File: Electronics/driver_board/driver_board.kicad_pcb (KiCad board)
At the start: 4 copper layers, 0 parts

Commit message: Initial placement
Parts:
- added C1: 0.1u, Capacitor_SMD:C_0402_1005Metric, F.Cu at (77.5, 67.5)
- added C11: 0.1u 150V, Capacitor_SMD:C_0805_2012Metric, F.Cu at (60.5, 123.5)
- added C18: 0.1u 150V, Capacitor_SMD:C_0805_2012Metric, F.Cu at (55.0, 136.0)
- added C2: 4.7u, Capacitor_SMD:C_0603_1608Metric, F.Cu at (91.0, 79.0)
- added C23: 1u, Capacitor_SMD:C_0402_1005Metric, F.Cu at (25.5, 102.0)
- added C24: 0.1u, Capacitor_SMD:C_0402_1005Metric, F.Cu at (27.0, 115.0)
- added C25: 0.1u, Capacitor_SMD:C_0402_1005Metric, F.Cu at (24.5, 93.0)
- added C26: 0.1u, Capacitor_SMD:C_0402_1005Metric, F.Cu at (27.0, 110.0)
- added C27: 1u, Capacitor_SMD:C_0402_1005Metric, F.Cu at (31.5, 102.0)
- added C28: 10u, Capacitor_SMD:C_0805_2012Metric, F.Cu at (32.5, 67.5)
- added C29: 10u, Capacitor_SMD:C_0805_2012Metric, F.Cu at (24.5, 90.0)
- added C3: 0.1u, Capacitor_SMD:C_0402_1005Metric, F.Cu at (77.5, 69.5)
- added C30: 10u, Capacitor_SMD:C_0805_2012Metric, F.Cu at (26.5, 108.5)
- added C31: 4.7u, Capacitor_SMD:C_0603_1608Metric, F.Cu at (160.0, 96.5)
- added C32: 4.7u, Capacitor_SMD:C_0603_1608Metric, F.Cu at (161.5, 108.5)
- added C33: 0.1u, Capacitor_SMD:C_0402_1005Metric, F.Cu at (161.5, 97.0)
- added C34: 0.1u, Capacitor_SMD:C_0402_1005Metric, F.Cu at (163.0, 109.0)
- added C35: 0.1u 150V, Capacitor_SMD:C_0805_2012Metric, F.Cu at (163.0, 90.5)
- added C36: 0.1u 150V, Capacitor_SMD:C_0805_2012Metric, F.Cu at (164.0, 113.0)
- added C37: 0.1u, Capacitor_SMD:C_0402_1005Metric, F.Cu at (187.5, 89.0)
- added C38: 0.1u, Capacitor_SMD:C_0402_1005Metric, F.Cu at (181.5, 82.0)
- added C39: 0.1u, Capacitor_SMD:C_0402_1005Metric, F.Cu at (183.5, 121.5)
- added C4: 0.1u, Capacitor_SMD:C_0402_1005Metric, F.Cu at (77.5, 71.5)
- added C40: 0.1u, Capacitor_SMD:C_0402_1005Metric, F.Cu at (176.5, 84.5)
- added C41: 0.1u, Capacitor_SMD:C_0402_1005Metric, F.Cu at (160.5, 76.0)
- added C5: 0.1u, Capacitor_SMD:C_0402_1005Metric, F.Cu at (77.5, 73.5)
- added C6: 4.7u, Capacitor_SMD:C_0603_1608Metric, F.Cu at (91.0, 81.5)
- added C7: 0.1u, Capacitor_SMD:C_0402_1005Metric, F.Cu at (77.5, 75.5)
- added C8: 0.1u, Capacitor_SMD:C_0402_1005Metric, F.Cu at (77.5, 77.0)
- added D1: SMAJ85A, Diode_SMD:D_SMA, F.Cu at (45.5, 112.0)
- added D2: SMAJ100CA, Diode_SMD:D_SMA, F.Cu at (186.5, 106.5)
- added J1: Conn_ST_STDC14, Connector_PinHeader_1.27mm:PinHeader_2x07_P1.27mm_Vertical_SMD, F.Cu at (63.0, 66.5)
- added NT1: NetTie_2, NetTie:NetTie-2_SMD_Pad0.5mm, F.Cu at (29.5, 115.5)
- added NT2: NetTie_2, NetTie:NetTie-2_SMD_Pad0.5mm, F.Cu at (157.5, 116.0)
- added Q1: IPF036N15NM6, Package_TO_SOT_SMD:TO-263-6, F.Cu at (59.0, 110.5)
- added Q2: IPF036N15NM6, Package_TO_SOT_SMD:TO-263-6, F.Cu at (80.0, 110.5)
- added Q3: IAUZ40N10S5N130, DWlib:Infineon_PG-TSDSON-8-33, B.Cu at (174.5, 95.0)
- added Q4: IAUZ40N10S5N130, DWlib:Infineon_PG-TSDSON-8-33, F.Cu at (176.5, 95.0)
- added Q5: IAUZ40N10S5N130, DWlib:Infineon_PG-TSDSON-8-33, B.Cu at (174.0, 108.0)
- added Q6: IAUZ40N10S5N130, DWlib:Infineon_PG-TSDSON-8-33, F.Cu at (176.5, 108.0)
- added R1: 150k, Resistor_SMD:R_0603_1608Metric, F.Cu at (58.0, 127.0)
- added R10: 4.7R, Resistor_SMD:R_0805_2012Metric, F.Cu at (166.0, 99.5)
- added R11: 4.7R, Resistor_SMD:R_0805_2012Metric, F.Cu at (164.5, 92.5)
- added R12: 4.7R, Resistor_SMD:R_0805_2012Metric, F.Cu at (167.5, 112.0)
- added R13: 4.7R, Resistor_SMD:R_0805_2012Metric, F.Cu at (167.0, 104.0)
- added R14: 7m, Resistor_SMD:R_2512_6332Metric, F.Cu at (181.0, 98.5)
- added R15: 267k, Resistor_SMD:R_0603_1608Metric, F.Cu at (187.0, 98.0)
- added R16: 10k, Resistor_SMD:R_0603_1608Metric, F.Cu at (187.0, 94.5)
- added R17: 1k, Resistor_SMD:R_0603_1608Metric, F.Cu at (185.5, 89.5)
- added R18: 267k, Resistor_SMD:R_0603_1608Metric, F.Cu at (186.5, 113.0)
- added R19: 10k, Resistor_SMD:R_0603_1608Metric, F.Cu at (186.5, 116.0)
- added R2: 11k, Resistor_SMD:R_0603_1608Metric, F.Cu at (60.5, 128.0)
- added R20: 1k, Resistor_SMD:R_0603_1608Metric, F.Cu at (184.0, 120.0)
- added R21: 100R, Resistor_SMD:R_0603_1608Metric, F.Cu at (178.5, 85.0)
- added R22: 267k, Resistor_SMD:R_0603_1608Metric, F.Cu at (157.0, 73.0)
- added R23: 10k, Resistor_SMD:R_0603_1608Metric, F.Cu at (157.0, 75.5)
- added R24: 1k, Resistor_SMD:R_0603_1608Metric, F.Cu at (157.0, 78.0)
- added R3: 100R, Resistor_SMD:R_0603_1608Metric, F.Cu at (58.0, 122.5)
- added R4: 2m, Resistor_SMD:R_1206_3216Metric, F.Cu at (50.0, 110.0)
- added R5: 4.7k, Resistor_SMD:R_0603_1608Metric, F.Cu at (66.0, 130.5)
- added R6: 100k, Resistor_SMD:R_0603_1608Metric, F.Cu at (64.5, 119.5)
- added R7: 10R, Resistor_SMD:R_0603_1608Metric, F.Cu at (67.0, 118.5)
- added R8: 100k, Resistor_SMD:R_0603_1608Metric, F.Cu at (67.5, 130.5)
- added R9: 11k, Resistor_SMD:R_0603_1608Metric, F.Cu at (64.5, 130.5)
- added SW1: TL3305, DWlib:SW_Push_1P1T_NO_E-Switch_TL3305AFxxxQG, F.Cu at (84.0, 81.0)
- added TP1: TestPoint, Connector_PinHeader_1.00mm:PinHeader_1x01_P1.00mm_Vertical, F.Cu at (92.0, 68.0)
- added TP2: TestPoint, Connector_PinHeader_1.00mm:PinHeader_1x01_P1.00mm_Vertical, F.Cu at (190.0, 87.5)
- added TP3: TestPoint, Connector_PinHeader_1.00mm:PinHeader_1x01_P1.00mm_Vertical, F.Cu at (184.0, 123.5)
- added TP4: TestPoint, Connector_PinHeader_1.00mm:PinHeader_1x01_P1.00mm_Vertical, F.Cu at (174.0, 86.5)
- added TP5: TestPoint, Connector_PinHeader_1.00mm:PinHeader_1x01_P1.00mm_Vertical, F.Cu at (160.5, 73.5)
- added U1: STM32G491CCT6, Package_QFP:LQFP-48_7x7mm_P0.5mm, F.Cu at (84.5, 72.0)
- added U2: TPS4810-Q1, DWlib:TI_VSSOP-19_3x5.1mm_P0.5mm, F.Cu at (65.0, 125.0)
- added U3: LMW78_12-0.5R, DWlib:Converter_DCDC_GAPTEC_LMW78_THT, F.Cu at (28.5, 72.0)
- added U4: LD1117S50CTR, Package_TO_SOT_SMD:SOT-223-3_TabPin2, F.Cu at (30.0, 91.0)
- added U5: LD39015M33R, Package_TO_SOT_SMD:SOT-23-5, F.Cu at (28.5, 102.5)
- added U6: REF3433TIDBVR, Package_TO_SOT_SMD:SOT-23-6, F.Cu at (26.5, 112.5)
- added U7: UCC27302ADRCR, DWlib:TI_VSON-10-1EP_3x3mm_P0.5mm_EP1.65x2.4mm, F.Cu at (164.5, 96.0)
- added U8: UCC27302ADRCR, DWlib:TI_VSON-10-1EP_3x3mm_P0.5mm_EP1.65x2.4mm, F.Cu at (166.0, 108.0)
- added U9: INA241A2xDDF, Package_TO_SOT_SMD:SOT-23-8, F.Cu at (178.5, 82.0)

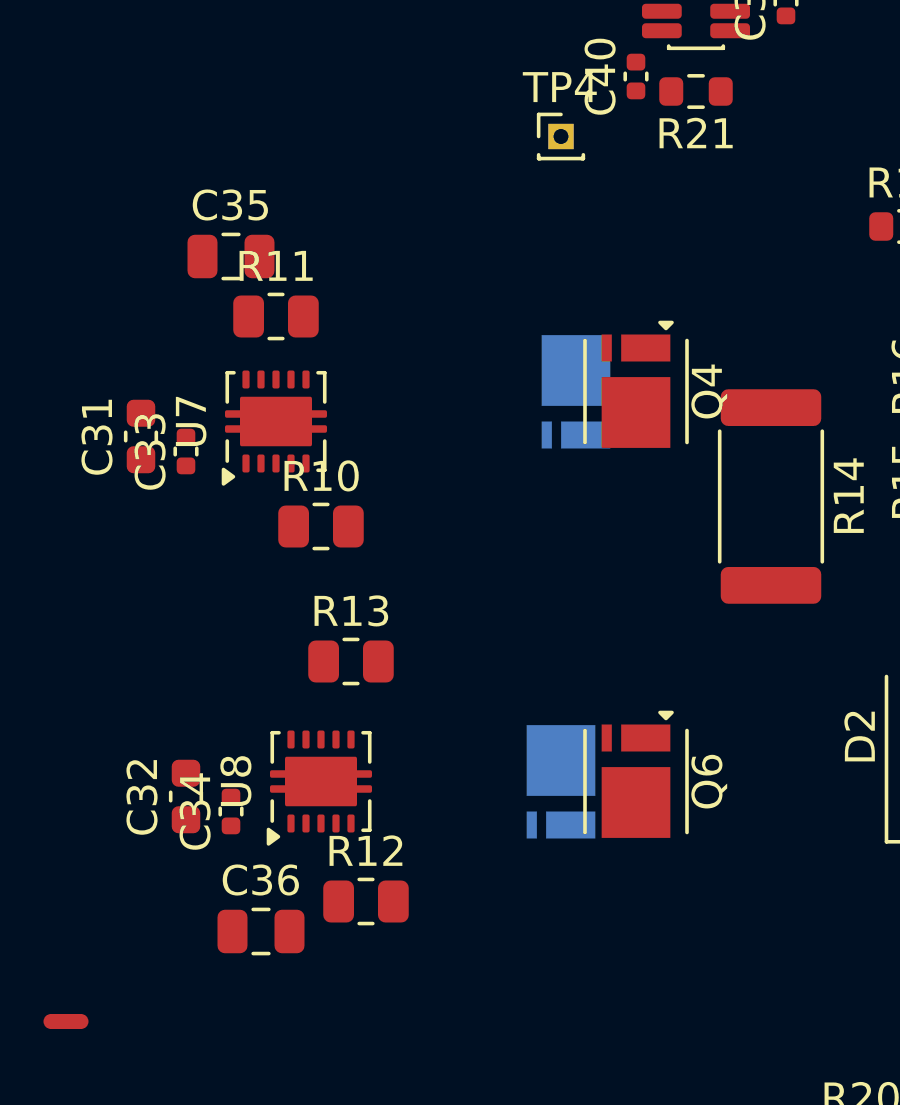
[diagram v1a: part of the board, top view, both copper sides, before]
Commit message: Added more capacitors, part numbers.
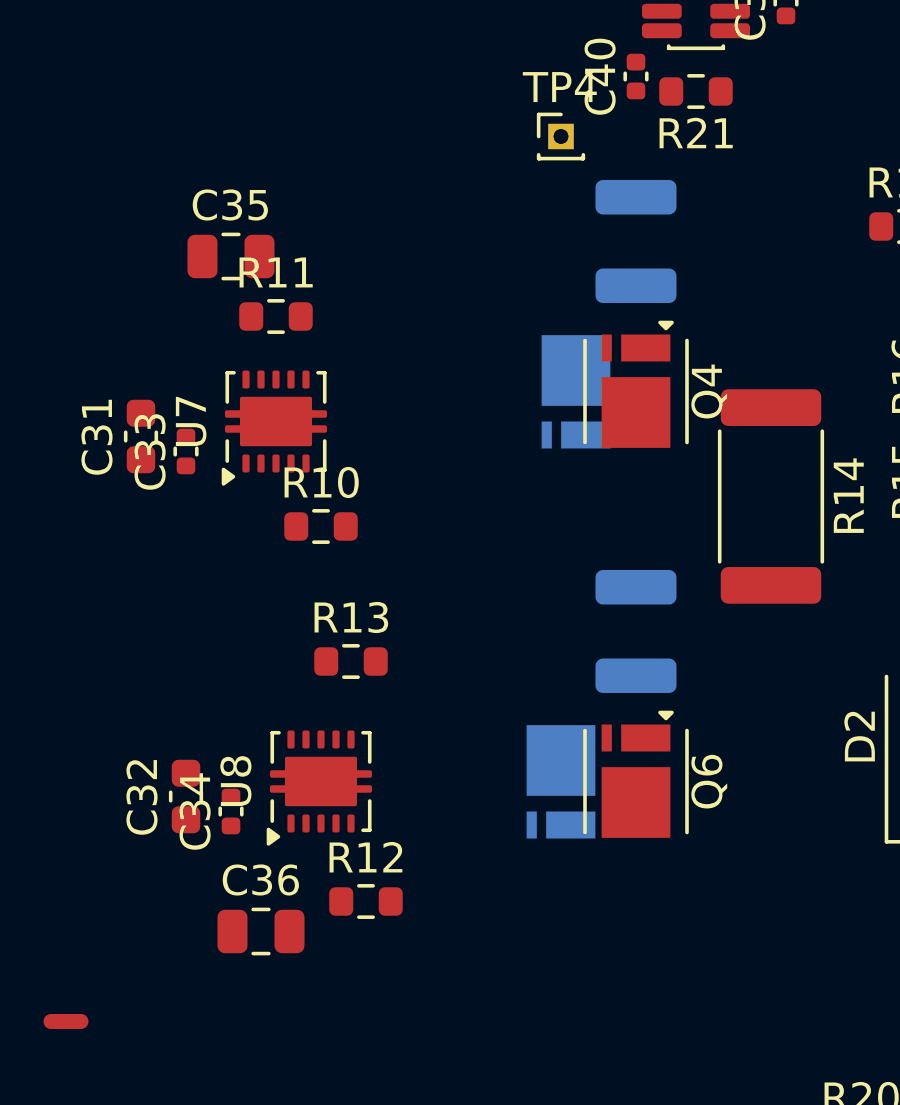
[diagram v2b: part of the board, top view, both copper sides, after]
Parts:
- added C42: 0.47u 200V, Capacitor_SMD:C_1210_3225Metric, B.Cu at (176.5, 90.0)
- added C43: 0.47u 200V, Capacitor_SMD:C_1210_3225Metric, B.Cu at (176.5, 103.0)
- R10, R11, R12, R13: footprint Resistor_SMD:R_0805_2012Metric -> Resistor_SMD:R_0603_1608Metric
